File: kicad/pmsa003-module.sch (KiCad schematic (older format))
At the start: 1 part, among them J1 Conn_02x15_Odd_Even

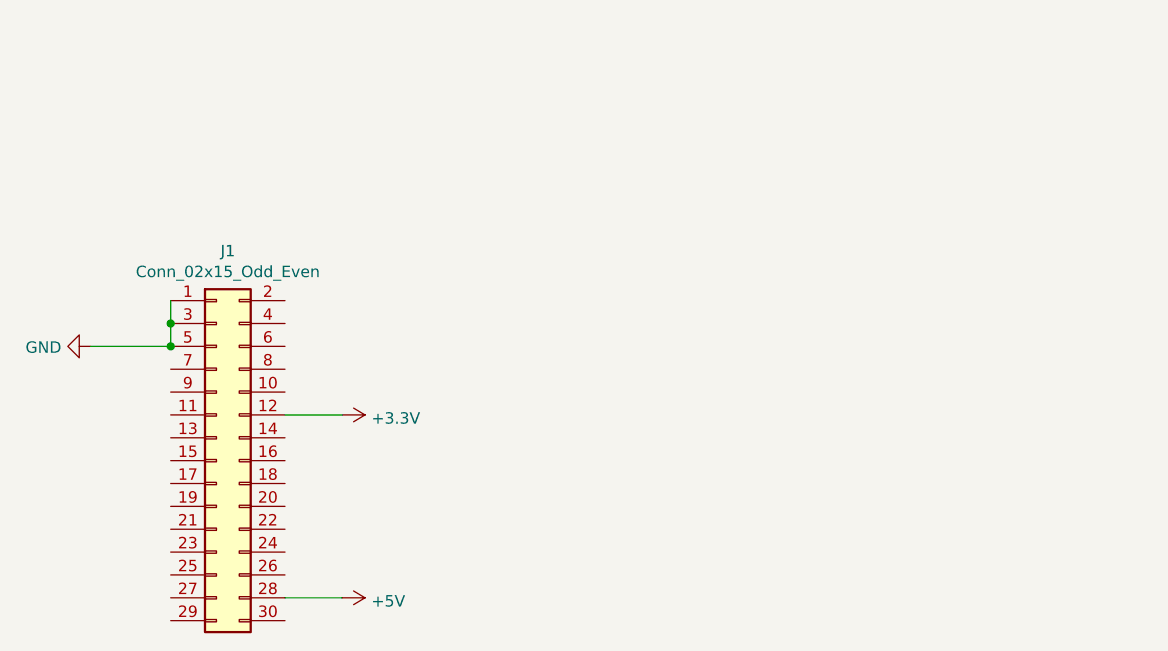
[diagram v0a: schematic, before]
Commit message: Add m5stack pinheader, route, etc.
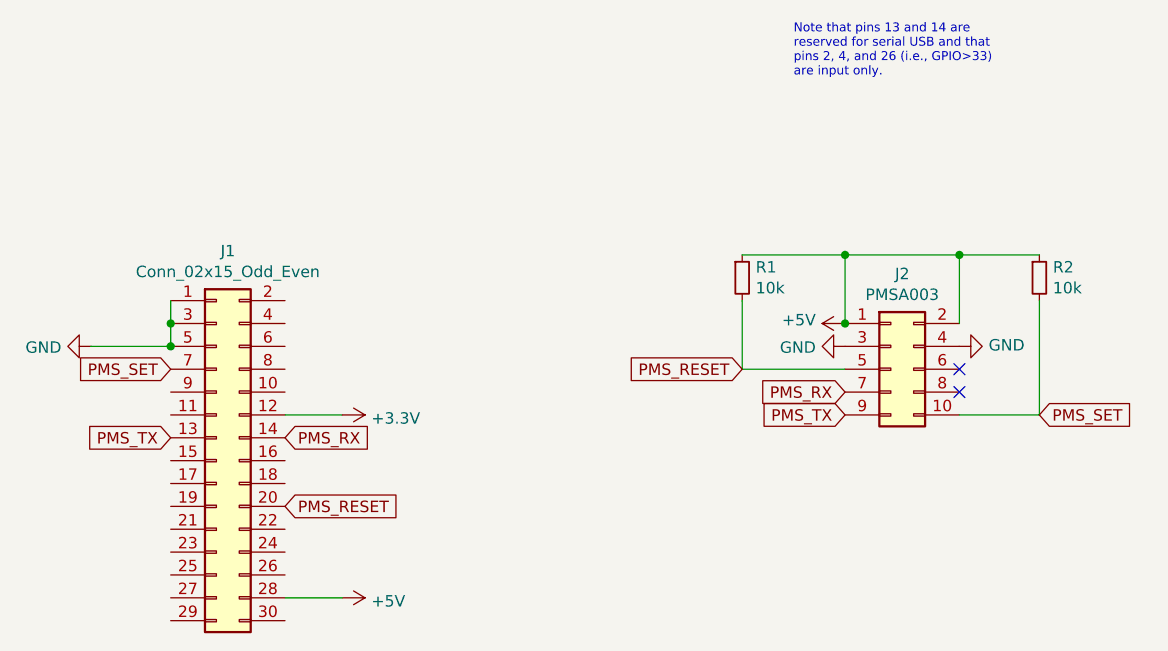
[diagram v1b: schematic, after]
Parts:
- added J2: PMSA003, lib:PMSA003, symbol Connector_Generic:Conn_02x05_Odd_Even
- added R1, R2: 10k, Resistor_SMD:R_0805_2012Metric, symbol Device:R_Small
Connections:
- net +5V: now also J2.1 (Pin_1), J2.2 (Pin_2), R1.1, R2.1
- net GND: now also J2.3 (Pin_3), J2.4 (Pin_4)
- net PMS_TX: now reaches J1.13 (Pin_13)
- net PMS_TX: now also J2.9 (Pin_9)
- net PMS_RX: now reaches J1.14 (Pin_14)
- net PMS_RX: now also J2.7 (Pin_7)
- net PMS_RESET: now reaches J1.20 (Pin_20)
- net PMS_RESET: now also J2.5 (Pin_5), R1.2
- net PMS_SET: now reaches J1.7 (Pin_7)
- net PMS_SET: now also J2.10 (Pin_10), R2.2
- no-connect marks 0 -> 2
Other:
- note added: "Note that pins 13 and 14 are\nreserved for serial USB and that\npins 2, 4, and 26 (i.e., GPIO>33)\nare input only."
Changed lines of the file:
@@
 encoding utf-8
 Sheet 1 1
-Title ""
-Date ""
-Rev ""
+Title "m5stack-pmsa003-module"
+Date "2021-02-06"
+Rev "v0.1"
 Comp ""
 Comment1 ""
@@
 $EndComp
 $Bitmap
-Pos 2250 1200
+Pos 2450 1275
 Scale 1.000000
 Data
@@
 Wire Wire Line
 	2250 2800 2000 2800
+$Comp
+L Connector_Generic:Conn_02x05_Odd_Even J2
+U 1 1 6019A810
+P 4650 2600
+F 0 "J2" H 4700 3017 50  0000 C CNN
+F 1 "PMSA003" H 4700 2926 50  0000 C CNN
+F 2 "lib:PMSA003" H 4650 2600 50  0001 C CNN
+F 3 "~" H 4650 2600 50  0001 C CNN
+	1    4650 2600
+	1    0    0    -1
+$EndComp
+$Comp
+L power:+5V #PWR0104
+U 1 1 6019E28E
+P 4450 2400
+F 0 "#PWR0104" H 4450 2250 50  0001 C CNN
+F 1 "+5V" V 4465 2528 50  0000 L CNN
+F 2 "" H 4450 2400 50  0001 C CNN
+F 3 "" H 4450 2400 50  0001 C CNN
+	1    4450 2400
+	0    -1   -1   0
+$EndComp
+Wire Wire Line
+	4450 2400 4450 2100
+Wire Wire Line
+	4450 2100 4950 2100
+Wire Wire Line
+	4950 2100 4950 2400
+Connection ~ 4450 2400
+$Comp
+L power:GND #PWR0106
+U 1 1 6019FC6F
+P 4950 2500
+F 0 "#PWR0106" H 4950 2250 50  0001 C CNN
+F 1 "GND" V 4955 2372 50  0000 R CNN
+F 2 "" H 4950 2500 50  0001 C CNN
+F 3 "" H 4950 2500 50  0001 C CNN
+	1    4950 2500
+	0    -1   -1   0
+$EndComp
+Connection ~ 4950 2100
+Text GLabel 5300 2800 2    50   Input ~ 0
+PMS_SET
+Text GLabel 4450 2800 0    50   Input ~ 0
+PMS_TX
+Text GLabel 4450 2700 0    50   Input ~ 0
+PMS_RX
+Text GLabel 4000 2600 0    50   Input ~ 0
+PMS_RESET
+NoConn ~ 4950 2600
+NoConn ~ 4950 2700
+Text GLabel 1500 2900 0    50   Input ~ 0
+PMS_TX
+Text GLabel 1500 2600 0    50   Input ~ 0
+PMS_SET
+Text GLabel 2000 2900 2    50   Input ~ 0
+PMS_RX
+Text GLabel 2000 3200 2    50   Input ~ 0
+PMS_RESET
+$Comp
+L Device:R_Small R2
+U 1 1 601A427D
+P 5300 2200
+F 0 "R2" H 5359 2246 50  0000 L CNN
+F 1 "10k" H 5359 2155 50  0000 L CNN
+F 2 "Resistor_SMD:R_0805_2012Metric" H 5300 2200 50  0001 C CNN
+F 3 "~" H 5300 2200 50  0001 C CNN
+	1    5300 2200
+	1    0    0    -1
+$EndComp
+$Comp
+L Device:R_Small R1
+U 1 1 601A5C5F
+P 4000 2200
+F 0 "R1" H 4059 2246 50  0000 L CNN
+F 1 "10k" H 4059 2155 50  0000 L CNN
+F 2 "Resistor_SMD:R_0805_2012Metric" H 4000 2200 50  0001 C CNN
+F 3 "~" H 4000 2200 50  0001 C CNN
+	1    4000 2200
+	1    0    0    -1
+$EndComp
+$Comp
+L power:GND #PWR0105
+U 1 1 6019EECA
+P 4450 2500
+F 0 "#PWR0105" H 4450 2250 50  0001 C CNN
+F 1 "GND" V 4455 2372 50  0000 R CNN
+F 2 "" H 4450 2500 50  0001 C CNN
+F 3 "" H 4450 2500 50  0001 C CNN
+	1    4450 2500
+	0    1    1    0
+$EndComp
+Wire Wire Line
+	4950 2100 5300 2100
+Wire Wire Line
+	5300 2300 5300 2800
+Wire Wire Line
+	4950 2800 5300 2800
+Wire Wire Line
+	4000 2100 4450 2100
+Connection ~ 4450 2100
+Wire Wire Line
+	4000 2300 4000 2600
+Wire Wire Line
+	4000 2600 4450 2600
+Text Notes 4225 1325 0    39   ~ 0
+Note that pins 13 and 14 are\nreserved for serial USB and that\npins 2, 4, and 26 (i.e., GPIO>33)\nare input only.
 $EndSCHEMATC
